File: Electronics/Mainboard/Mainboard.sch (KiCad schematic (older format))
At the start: 13 parts, among them J1 609-5192-ND, J2 DB25_Male_MountingHoles, J3 609-5192-ND, J4 609-5192-ND, U14 LM75C

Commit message: Mainboard layout and schematic done
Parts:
- added JP29: Jumper, Jumper:SolderJumper-2_P1.3mm_Open_TrianglePad1.0x1.5mm, symbol Device:Jumper
- added LOGO1: Logo_Open_Hardware_Small, Symbol:OSHW-Logo2_24.3x20mm_SilkScreen, symbol Graphic:Logo_Open_Hardware_Small
- added SYM1: SYM_ESD_Large, Symbol:ESD-Logo_13.2x12mm_SilkScreen, symbol Graphic:SYM_ESD_Large
- added TP15, TP16: TestPoint, TestPoint:TestPoint_Pad_D1.5mm, symbol Connector:TestPoint
- C138: LCSC (none) -> C14663
- C139: value C_Small -> 100n; LCSC (none) -> C24497
- R29: footprint Capacitor_SMD:C_0805_2012Metric_Pad1.15x1.40mm_HandSolder -> Resistor_SMD:R_0805_2012Metric; LCSC (none) -> C17673
- R30: value R_Small -> 1M2; LCSC (none) -> C22107
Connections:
- net +15V: now also TP15.1
- net -15V: now also TP16.1
- net GND: now also JP29.2
- net Shield: now also JP29.1
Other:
- moved on the sheet: C139, N1, R30
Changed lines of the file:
@@
 L Mechanical:Housing N1
 U 1 1 5D85575A
-P 1000 7450
-F 0 "N1" H 1153 7484 50  0000 L CNN
-F 1 "Housing" H 1153 7393 50  0000 L CNN
-F 2 "STM_Custom_Lib:Hammond_1455P1601" H 1050 7500 50  0001 C CNN
-F 3 "https://www.reichelt.de/profilgehaeuse-1455-p-160-x-120-x-30-5-mm-silber-1455p1601-p221381.html?&trstct=pol_6" H 1050 7500 50  0001 C CNN
-	1    1000 7450
+P 1500 7150
+F 0 "N1" H 1653 7184 50  0000 L CNN
+F 1 "Housing" H 1653 7093 50  0000 L CNN
+F 2 "STM_Custom_Lib:Hammond_1455P1601" H 1550 7200 50  0001 C CNN
+F 3 "https://www.reichelt.de/profilgehaeuse-1455-p-160-x-120-x-30-5-mm-silber-1455p1601-p221381.html?&trstct=pol_6" H 1550 7200 50  0001 C CNN
+	1    1500 7150
 	1    0    0    -1
 $EndComp
@@
 ADC_IN-
 Wire Wire Line
-	10200 3750 9950 3750
+	10200 3750 10100 3750
 Wire Wire Line
 	10200 3950 10050 3950
@@
 	10050 4550 10050 4850
 Wire Wire Line
-	9950 3850 10200 3850
+	9700 3850 9950 3850
 Wire Wire Line
 	10200 4050 9950 4050
@@
 Wire Wire Line
 	10200 4450 9950 4450
-Text Label 9950 3850 2    50   ~ 0
+Text Label 9700 3850 2    50   ~ 0
 +15V
-Text Label 9950 3750 2    50   ~ 0
+Text Label 9700 3750 2    50   ~ 0
 -15V
 Text Label 9950 4050 2    50   ~ 0
@@
 F 2 "Capacitor_SMD:C_0603_1608Metric_Pad1.05x0.95mm_HandSolder" H 6138 6650 50  0001 C CNN
 F 3 "~" H 6100 6800 50  0001 C CNN
+F 4 "C14663" H 6100 6800 50  0001 C CNN "LCSC"
 	1    6100 6800
 	1    0    0    -1
@@
 F 0 "R29" V 4550 4900 50  0000 C CNN
 F 1 "4k7" V 4550 5100 50  0000 C CNN
-F 2 "Capacitor_SMD:C_0805_2012Metric_Pad1.15x1.40mm_HandSolder" V 4580 5000 50  0001 C CNN
+F 2 "Resistor_SMD:R_0805_2012Metric" V 4580 5000 50  0001 C CNN
 F 3 "~" H 4650 5000 50  0001 C CNN
+F 4 "C17673" H 4650 5000 50  0001 C CNN "LCSC"
 	1    4650 5000
 	0    1    1    0
@@
 L Device:C_Small C139
 U 1 1 5F326529
-P 2400 750
-F 0 "C139" V 2263 750 50  0000 C CNN
-F 1 "C_Small" V 2262 750 50  0001 C CNN
-F 2 "Capacitor_SMD:C_1206_3216Metric_Pad1.42x1.75mm_HandSolder" H 2400 750 50  0001 C CNN
-F 3 "~" H 2400 750 50  0001 C CNN
-	1    2400 750
+P 2600 750
+F 0 "C139" V 2463 750 50  0000 C CNN
+F 1 "100n" V 2462 750 50  0001 C CNN
+F 2 "Capacitor_SMD:C_1206_3216Metric_Pad1.42x1.75mm_HandSolder" H 2600 750 50  0001 C CNN
+F 3 "~" H 2600 750 50  0001 C CNN
+F 4 "C24497" H 2600 750 50  0001 C CNN "LCSC"
+	1    2600 750
 	0    1    1    0
 $EndComp
 Wire Wire Line
-	2300 750  2200 750
+	2500 750  2200 750
 Wire Wire Line
 	2200 750  2200 900
@@
 L Device:R_Small R30
 U 1 1 5F3363D7
-P 2400 1050
-F 0 "R30" V 2296 1050 50  0000 C CNN
-F 1 "R_Small" V 2295 1050 50  0001 C CNN
-F 2 "Resistor_SMD:R_1206_3216Metric_Pad1.42x1.75mm_HandSolder" H 2400 1050 50  0001 C CNN
-F 3 "~" H 2400 1050 50  0001 C CNN
-	1    2400 1050
+P 2600 1050
+F 0 "R30" V 2496 1050 50  0000 C CNN
+F 1 "1M2" V 2495 1050 50  0001 C CNN
+F 2 "Resistor_SMD:R_1206_3216Metric_Pad1.42x1.75mm_HandSolder" H 2600 1050 50  0001 C CNN
+F 3 "~" H 2600 1050 50  0001 C CNN
+F 4 "C22107" H 2600 1050 50  0001 C CNN "LCSC"
+	1    2600 1050
 	0    1    1    0
 $EndComp
 Wire Wire Line
-	2300 1050 2200 1050
+	2500 1050 2200 1050
 Wire Wire Line
 	2200 1050 2200 900
 Connection ~ 2200 900
 Wire Wire Line
-	2500 1050 2600 1050
-Wire Wire Line
-	2600 1050 2600 900
-Wire Wire Line
-	2600 750  2500 750
-Wire Wire Line
-	2600 900  2700 900
-Connection ~ 2600 900
-Wire Wire Line
-	2600 900  2600 750
-Text Label 2700 900  0    50   ~ 0
-GND
+	2700 1050 3000 1050
+Wire Wire Line
+	3000 1050 3000 900
+Wire Wire Line
+	3000 750  2700 750
+Wire Wire Line
+	3000 900  3100 900
+Connection ~ 3000 900
+Wire Wire Line
+	3000 900  3000 750
+Text Label 3100 900  0    50   ~ 0
+GND
+$Comp
+L Connector:TestPoint TP?
+U 1 1 5F1E2DD9
+P 10100 3600
+AR Path="/5D61D488/5F1E2DD9" Ref="TP?"  Part="1"
+AR Path="/5F1E2DD9" Ref="TP16"  Part="1"
+F 0 "TP16" H 10100 3800 50  0000 L CNN
+F 1 "TestPoint" H 10158 3627 50  0001 L CNN
+F 2 "TestPoint:TestPoint_Pad_D1.5mm" H 10300 3600 50  0001 C CNN
+F 3 "~" H 10300 3600 50  0001 C CNN
+	1    10100 3600
+	1    0    0    -1
+$EndComp
+Wire Wire Line
+	10100 3600 10100 3750
+Connection ~ 10100 3750
+Wire Wire Line
+	10100 3750 9700 3750
+$Comp
+L Connector:TestPoint TP?
+U 1 1 5F210FA7
+P 9950 3600
+AR Path="/5D61D488/5F210FA7" Ref="TP?"  Part="1"
+AR Path="/5F210FA7" Ref="TP15"  Part="1"
+F 0 "TP15" H 9900 3800 50  0000 L CNN
+F 1 "TestPoint" H 10008 3627 50  0001 L CNN
+F 2 "TestPoint:TestPoint_Pad_D1.5mm" H 10150 3600 50  0001 C CNN
+F 3 "~" H 10150 3600 50  0001 C CNN
+	1    9950 3600
+	1    0    0    -1
+$EndComp
+Wire Wire Line
+	9950 3600 9950 3850
+Connection ~ 9950 3850
+Wire Wire Line
+	9950 3850 10200 3850
+$Comp
+L Graphic:SYM_ESD_Large SYM1
+U 1 1 5F433C50
+P 3550 7150
+F 0 "SYM1" H 3550 7350 50  0001 C CNN
+F 1 "SYM_ESD_Large" H 3550 6900 50  0001 C CNN
+F 2 "Symbol:ESD-Logo_13.2x12mm_SilkScreen" H 3545 7120 50  0001 C CNN
+F 3 "~" H 3545 7120 50  0001 C CNN
+	1    3550 7150
+	1    0    0    -1
+$EndComp
+$Comp
+L Device:Jumper JP29
+U 1 1 5F441C4B
+P 2350 300
+F 0 "JP29" H 2350 473 50  0000 C CNN
+F 1 "Jumper" H 2350 473 50  0001 C CNN
+F 2 "Jumper:SolderJumper-2_P1.3mm_Open_TrianglePad1.0x1.5mm" H 2350 300 50  0001 C CNN
+F 3 "~" H 2350 300 50  0001 C CNN
+	1    2350 300
+	1    0    0    -1
+$EndComp
+Wire Wire Line
+	2050 300  1400 300
+Wire Wire Line
+	1400 300  1400 900
+Wire Wire Line
+	2650 300  3000 300
+Wire Wire Line
+	3000 300  3000 750
+Connection ~ 3000 750
+$Comp
+L Graphic:Logo_Open_Hardware_Small LOGO1
+U 1 1 5F466E28
+P 2850 7200
+F 0 "LOGO1" H 2850 7475 50  0001 C CNN
+F 1 "Logo_Open_Hardware_Small" H 2850 6975 50  0001 C CNN
+F 2 "Symbol:OSHW-Logo2_24.3x20mm_SilkScreen" H 2850 7200 50  0001 C CNN
+F 3 "~" H 2850 7200 50  0001 C CNN
+	1    2850 7200
+	1    0    0    -1
+$EndComp
 $EndSCHEMATC

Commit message: Added images
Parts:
- J1, J3, J4: Digikey 609-5192-ND -> (none); Reichelt (none) -> RND 205-00769
- J2: Reichelt (none) -> D-SUB ST 25US
- N1: Reichelt (none) -> 1455P1601
- U14: Reichelt (none) -> LM 75 SMD
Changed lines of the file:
@@
 F 2 "STM_Custom_Lib:Hammond_1455P1601" H 1550 7200 50  0001 C CNN
 F 3 "https://www.reichelt.de/profilgehaeuse-1455-p-160-x-120-x-30-5-mm-silber-1455p1601-p221381.html?&trstct=pol_6" H 1550 7200 50  0001 C CNN
+F 4 "1455P1601" H 1500 7150 50  0001 C CNN "Reichelt"
 	1    1500 7150
 	1    0    0    -1
@@
 F 2 "Connector_Dsub:DSUB-25_Male_Horizontal_P2.77x2.84mm_EdgePinOffset4.94mm_Housed_MountingHolesOffset7.48mm" H 1400 2600 50  0001 C CNN
 F 3 " ~" H 1400 2600 50  0001 C CNN
+F 4 "D-SUB ST 25US" H 1400 2600 50  0001 C CNN "Reichelt"
 	1    1400 2600
 	-1   0    0    1
@@
 F 2 "STM_Custom_Lib:DSUB-9_Amphenol_LD09S33E4GV00LF" H 10500 1750 50  0001 C CNN
 F 3 " ~" H 10500 1750 50  0001 C CNN
-F 4 "609-5192-ND " H 10500 1750 50  0001 C CNN "Digikey"
+F 4 "" H 10500 1750 50  0001 C CNN "Digikey"
+F 5 "RND 205-00769" H 10500 1750 50  0001 C CNN "Reichelt"
 	1    10500 1750
 	1    0    0    -1
@@
 F 2 "STM_Custom_Lib:DSUB-9_Amphenol_LD09S33E4GV00LF" H 9400 5400 50  0001 C CNN
 F 3 " ~" H 9400 5400 50  0001 C CNN
-F 4 "609-5192-ND " H 9400 5400 50  0001 C CNN "Digikey"
+F 4 "" H 9400 5400 50  0001 C CNN "Digikey"
+F 5 "RND 205-00769" H 9400 5400 50  0001 C CNN "Reichelt"
 	1    9400 5400
 	1    0    0    -1
@@
 F 2 "STM_Custom_Lib:DSUB-9_Amphenol_LD09S33E4GV00LF" H 10500 4150 50  0001 C CNN
 F 3 " ~" H 10500 4150 50  0001 C CNN
-F 4 "609-5192-ND " H 10500 4150 50  0001 C CNN "Digikey"
+F 4 "" H 10500 4150 50  0001 C CNN "Digikey"
+F 5 "RND 205-00769" H 10500 4150 50  0001 C CNN "Reichelt"
 	1    10500 4150
 	1    0    0    -1
@@
 F 2 "Package_SO:SOIC-8_3.9x4.9mm_P1.27mm" H 5400 6800 50  0001 C CNN
 F 3 "http://www.ti.com/lit/ds/symlink/lm75b.pdf" H 5400 6800 50  0001 C CNN
+F 4 "LM 75 SMD" H 5400 6800 50  0001 C CNN "Reichelt"
 	1    5400 6800
 	1    0    0    -1

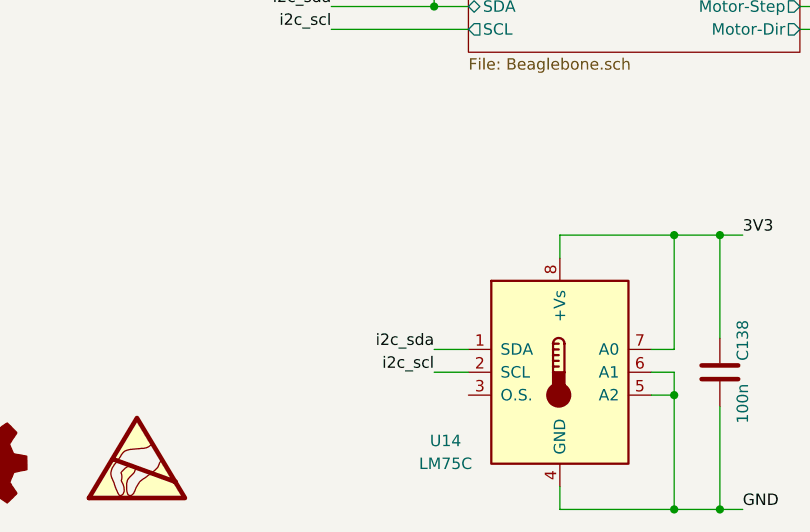
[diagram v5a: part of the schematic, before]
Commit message: Added i2c address to mainboard lm75
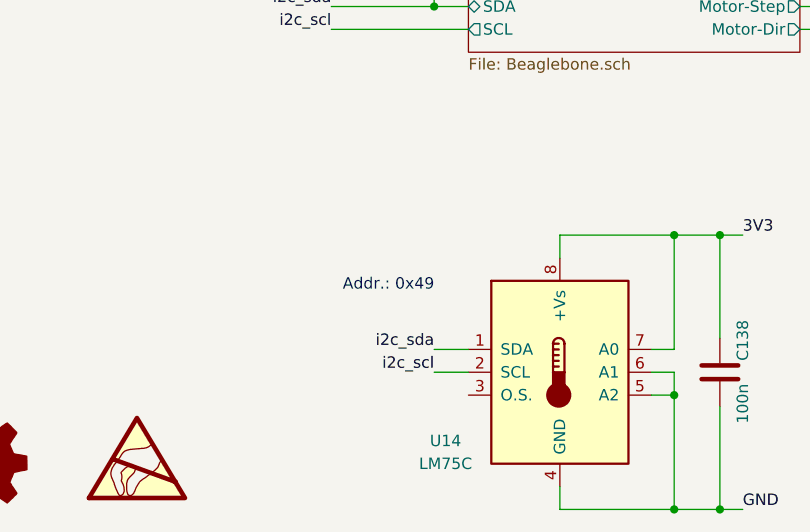
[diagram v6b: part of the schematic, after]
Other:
- note added: "Addr.: 0x49"
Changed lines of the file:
@@
 	1    0    0    -1
 $EndComp
+Text Notes 4450 6450 0    50   ~ 0
+Addr.: 0x49
 $EndSCHEMATC
